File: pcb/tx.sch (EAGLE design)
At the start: 54 parts, among them U3 MCP73831T-2ACI/OT, Y1 CRYSTAL-26MHZSMD-3.2X2.5

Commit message: added holes to button
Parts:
- U$10: value 324_SW -> 324_SW324_SWITCH_FOOT_HOLE; device 3pos_slide_switch:324_SW -> 3pos_slide_switch:324_SW324_SWITCH_FOOT_HOLE
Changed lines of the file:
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@@
 <part name="GND23" library="supply1" library_urn="urn:adsk.eagle:library:371" deviceset="GND" device=""/>
 <part name="GND24" library="supply1" library_urn="urn:adsk.eagle:library:371" deviceset="GND" device=""/>
-<part name="U$10" library="3pos_slide_switch" deviceset="324_SW" device=""/>
+<part name="U$10" library="3pos_slide_switch" deviceset="324_SW" device="324_SWITCH_FOOT_HOLE" value="324_SW324_SWITCH_FOOT_HOLE"/>
 <part name="R9" library="joyAnalog" deviceset="RESISTOR" device="0805-RES" value="22K"/>
 <part name="GND25" library="supply1" library_urn="urn:adsk.eagle:library:371" deviceset="GND" device=""/>

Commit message: laser works
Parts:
- R6, R7: value 22K -> 5.1K
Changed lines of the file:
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@@
 <part name="LED1" library="joyAnalog" deviceset="LED" device="CHIP-LED0805"/>
 <part name="GND18" library="clock" deviceset="GND" device=""/>
-<part name="R6" library="SparkFun-Passives" deviceset="RESISTOR" device="0805-RES" value="22K"/>
-<part name="R7" library="SparkFun-Passives" deviceset="RESISTOR" device="0805-RES" value="22K"/>
+<part name="R6" library="SparkFun-Passives" deviceset="RESISTOR" device="0805-RES" value="5.1K"/>
+<part name="R7" library="SparkFun-Passives" deviceset="RESISTOR" device="0805-RES" value="5.1K"/>
 <part name="+3V3" library="supply1" library_urn="urn:adsk.eagle:library:371" deviceset="+3V3" device=""/>
 <part name="+3V4" library="supply1" library_urn="urn:adsk.eagle:library:371" deviceset="+3V3" device=""/>

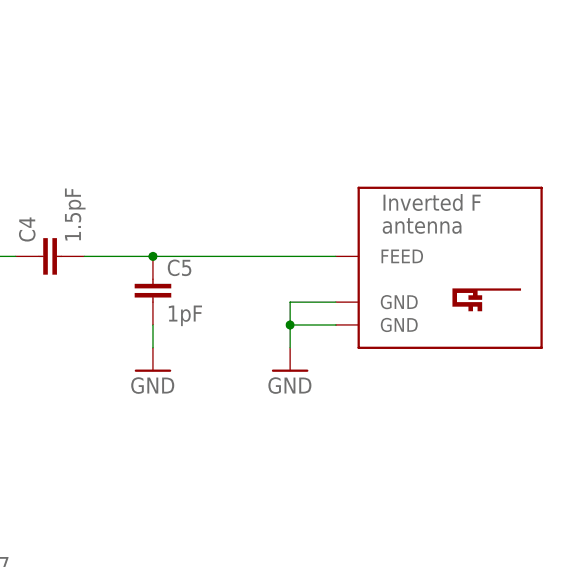
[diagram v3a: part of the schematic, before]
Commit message: updated PCB, firmware sleep working
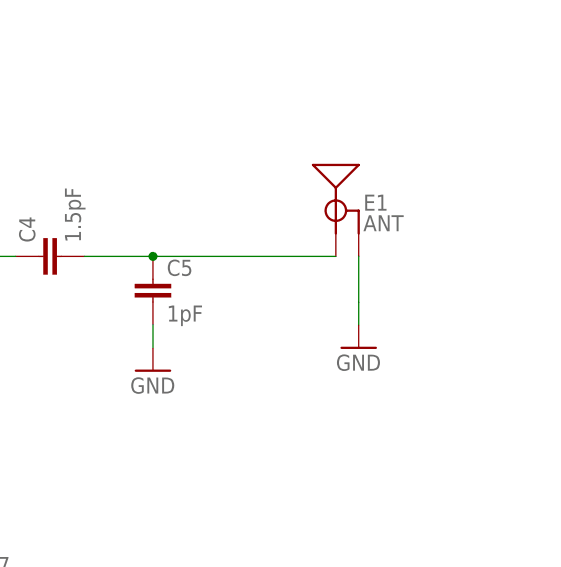
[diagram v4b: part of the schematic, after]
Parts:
- removed U$4: INVERTED_F_ANTENNA+0, antenna:INVERTED_F_ANTENNA+0
- added E1: ANT, SparkFun-RF:ANTENNA-GROUNDEDTRACE-15.2MM
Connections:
- net GND: now also E1.GND; no longer U$4.GND, U$4.GND@1
- net N$5: now also E1.SIGNAL; no longer U$4.FEED
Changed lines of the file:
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@@
 <part name="U$2" library="exixe_pogo" deviceset="STM32F030F4" device=""/>
 <part name="U1" library="Adafruit VL53L0X" deviceset="VL53L0X" device=""/>
-<part name="U$4" library="antenna" deviceset="INVERTED_F_ANTENNA" device="+0"/>
 <part name="U$5" library="L1" deviceset="M3_MOUNTING_HOLE" device=""/>
 <part name="U$6" library="L1" deviceset="M3_MOUNTING_HOLE" device=""/>
@@
 <part name="TP1" library="testpad" library_urn="urn:adsk.eagle:library:385" deviceset="TP" device="TP12R" package3d_urn="urn:adsk.eagle:package:27963/1" value="TPTP12R"/>
 <part name="TP2" library="testpad" library_urn="urn:adsk.eagle:library:385" deviceset="TP" device="TP12R" package3d_urn="urn:adsk.eagle:package:27963/1" value="TPTP12R"/>
+<part name="E1" library="SparkFun-RF" deviceset="ANTENNA-GROUNDED" device="TRACE-15.2MM" value="ANT"/>
 </parts>
 <sheets>
@@
 <instance part="U$2" gate="G$1" x="-15.24" y="-58.42"/>
 <instance part="U1" gate="G$1" x="45.72" y="25.4"/>
-<instance part="U$4" gate="G$1" x="215.9" y="-58.42"/>
 <instance part="U$5" gate="G$1" x="-246.38" y="63.5"/>
 <instance part="U$6" gate="G$1" x="-246.38" y="48.26"/>
@@
 <instance part="GND17" gate="1" x="-226.06" y="-63.5"/>
 <instance part="LED1" gate="G$1" x="-264.16" y="-45.72"/>
-<instance part="GND18" gate="1" x="203.2" y="-68.58"/>
+<instance part="GND18" gate="1" x="210.82" y="-66.04"/>
 <instance part="R6" gate="G$1" x="17.78" y="33.02" rot="R90"/>
 <instance part="R7" gate="G$1" x="7.62" y="30.48" rot="R90"/>
@@
 <instance part="TP1" gate="G$1" x="25.4" y="10.16" rot="R180"/>
 <instance part="TP2" gate="G$1" x="-40.64" y="-55.88" rot="R90"/>
+<instance part="E1" gate="G$1" x="208.28" y="-45.72"/>
 </instances>
 <busses>
@@
 </segment>
 <segment>
-<pinref part="U$4" gate="G$1" pin="GND@1"/>
 <pinref part="GND18" gate="1" pin="GND"/>
-<wire x1="208.28" y1="-63.5" x2="203.2" y2="-63.5" width="0.1524" layer="91"/>
-<wire x1="203.2" y1="-63.5" x2="203.2" y2="-66.04" width="0.1524" layer="91"/>
-<pinref part="U$4" gate="G$1" pin="GND"/>
-<wire x1="208.28" y1="-60.96" x2="203.2" y2="-60.96" width="0.1524" layer="91"/>
-<wire x1="203.2" y1="-60.96" x2="203.2" y2="-63.5" width="0.1524" layer="91"/>
-<junction x="203.2" y="-63.5"/>
+<wire x1="210.82" y1="-60.96" x2="210.82" y2="-63.5" width="0.1524" layer="91"/>
+<pinref part="E1" gate="G$1" pin="GND"/>
+<wire x1="210.82" y1="-60.96" x2="210.82" y2="-55.88" width="0.1524" layer="91"/>
 </segment>
 <segment>
@@
 <wire x1="187.96" y1="-55.88" x2="208.28" y2="-55.88" width="0.1524" layer="91"/>
 <junction x="187.96" y="-55.88"/>
-<pinref part="U$4" gate="G$1" pin="FEED"/>
-</segment>
-</net>
+<pinref part="E1" gate="G$1" pin="SIGNAL"/>
+</segment>
+</net>
